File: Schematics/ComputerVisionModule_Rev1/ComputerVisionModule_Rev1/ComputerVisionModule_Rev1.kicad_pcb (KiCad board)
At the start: 4 copper layers, 7 parts, among them J1 DF40C-40DP-0.4V_51_, SW1 SW_Push

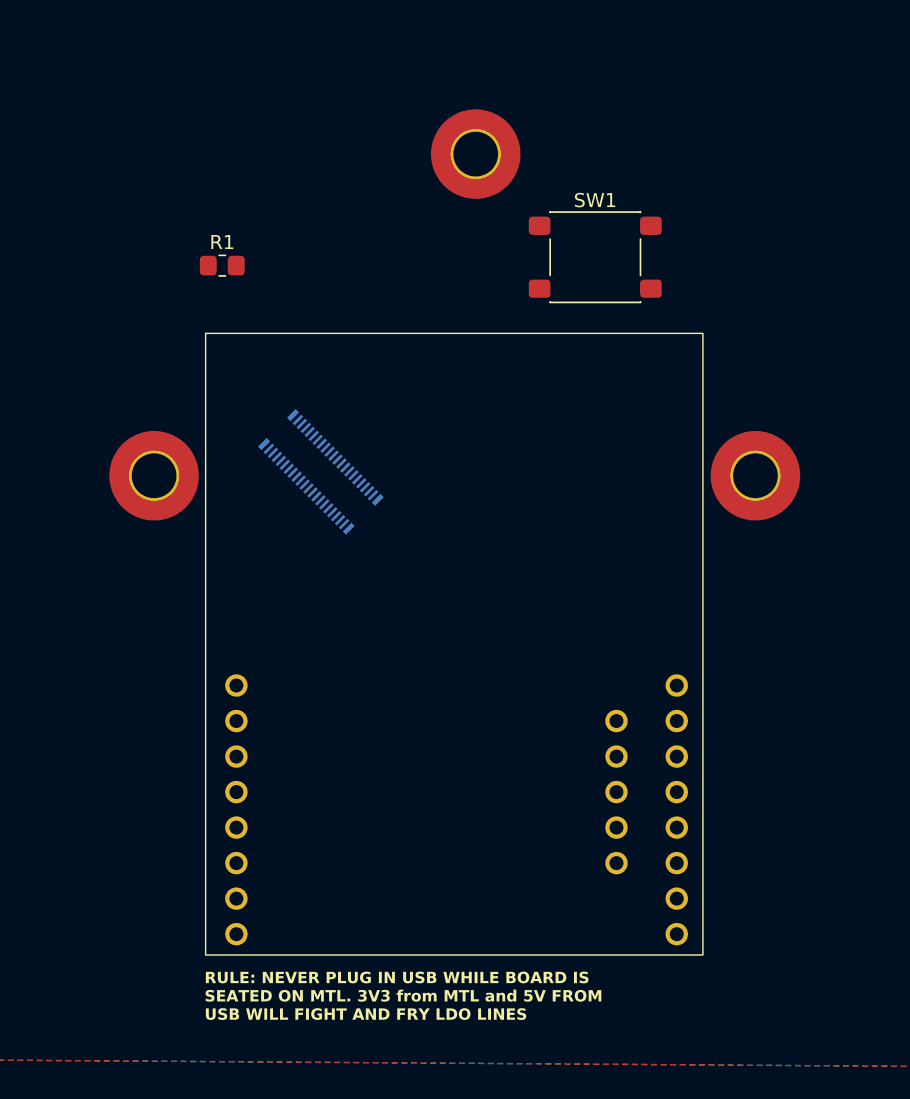
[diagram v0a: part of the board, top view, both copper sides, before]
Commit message: Added Bottom Module GPIO Demo board
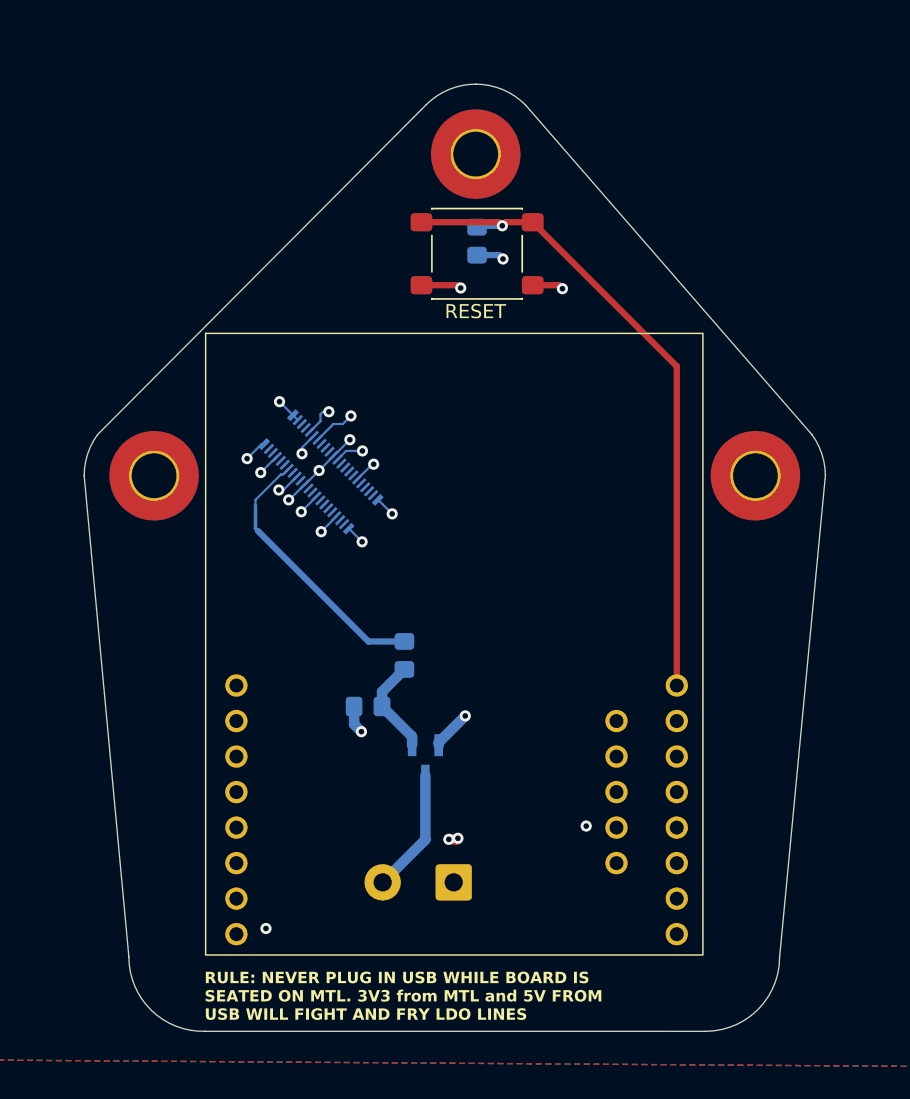
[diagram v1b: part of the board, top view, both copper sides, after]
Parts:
- added J2: Screw_Terminal_01x02, TerminalBlock_Phoenix:TerminalBlock_Phoenix_MKDS-1,5-2-5.08_1x02_P5.08mm_Horizontal, B.Cu at (121.1, 140.1)
- added R2: 100, Resistor_SMD:R_0805_2012Metric_Pad1.20x1.40mm_HandSolder, B.Cu at (117.6, 123.8)
- added R3: 10k, Resistor_SMD:R_0805_2012Metric_Pad1.20x1.40mm_HandSolder, B.Cu at (115.0, 127.5)
- added U2: BSS138, BSS138:SOT-23_3L_ONS-M, B.Cu at (119.1, 131.3)
- R1: moved to B.Cu
- moved R1 18.3 mm to (122.8, 94.2), turned to 90 degrees
- moved SW1 8.46 mm to (122.8, 95.1)
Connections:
- J1 pad 12: unconnected-(J1-Pad12) -> Net-(J1-Pad12)
- U1 pad 1: Net-(U1-3V3-Pad1) -> +3V3
- U1 pad 7: Net-(U1-3V3-Pad1) -> +3V3
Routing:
- net Net-(U1-RST): track 0.00 -> 47.4 mm, vias 0 -> 1
- net Net-(U1-RX): track 0.00 -> 37.6 mm, vias 0 -> 1
- net Net-(U1-TX): track 0.00 -> 30.9 mm, vias 0 -> 1
- net GND: track 0.00 -> 29.6 mm, vias 0 -> 15
- net Net-(J1-Pad12): track 0.00 -> 19.3 mm
- net +3V3: track 0.00 -> 16.5 mm, vias 0 -> 8
- net Net-(J2-Pin_2): track 0.00 -> 8.89 mm
- net Net-(U2-G): track 0.00 -> 6.97 mm
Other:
- board outline added: 53 x 67.7 mm
- board text added: "RESET"
